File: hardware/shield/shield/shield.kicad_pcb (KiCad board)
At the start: 2 copper layers, 66 x 53.3 mm, 4 parts, among them J1 Power, J2 Digital/PWM, J3 Analog, J4 Digital/PWM

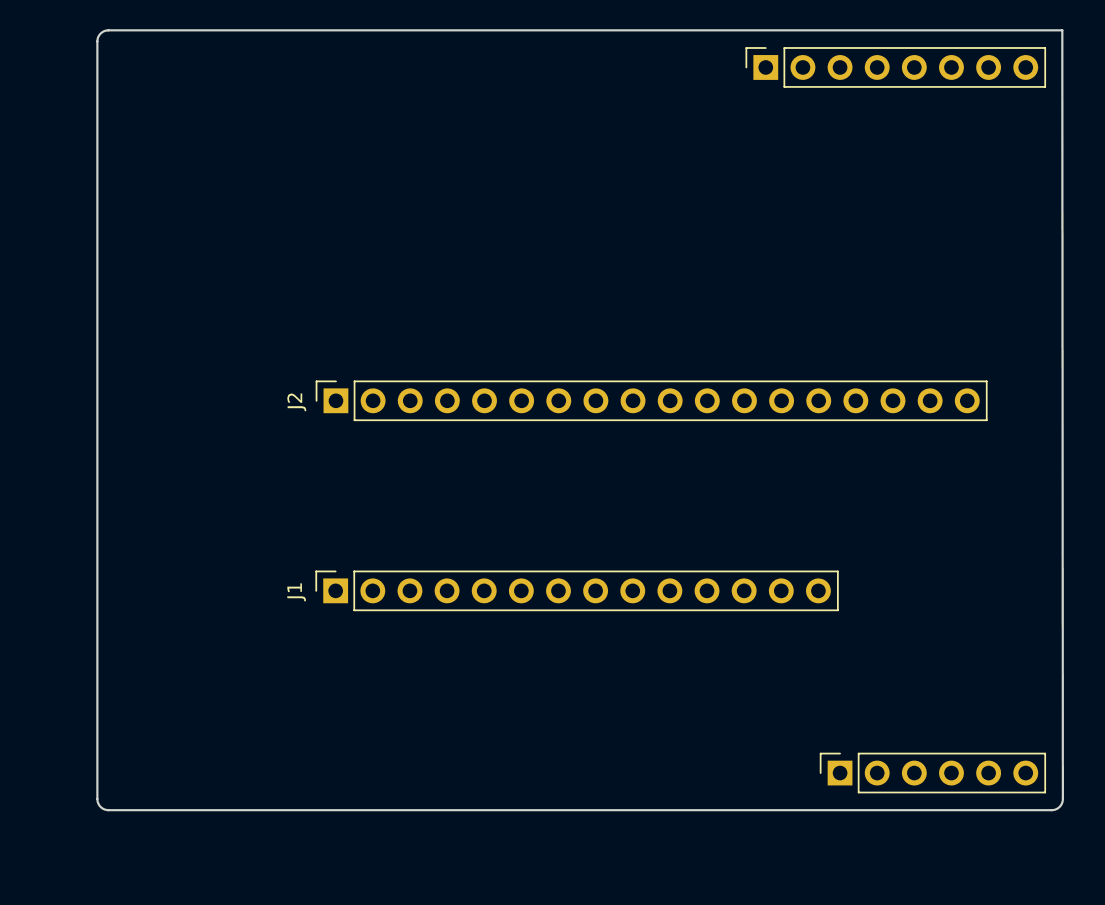
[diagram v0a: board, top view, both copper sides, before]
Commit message: add pins for in/out
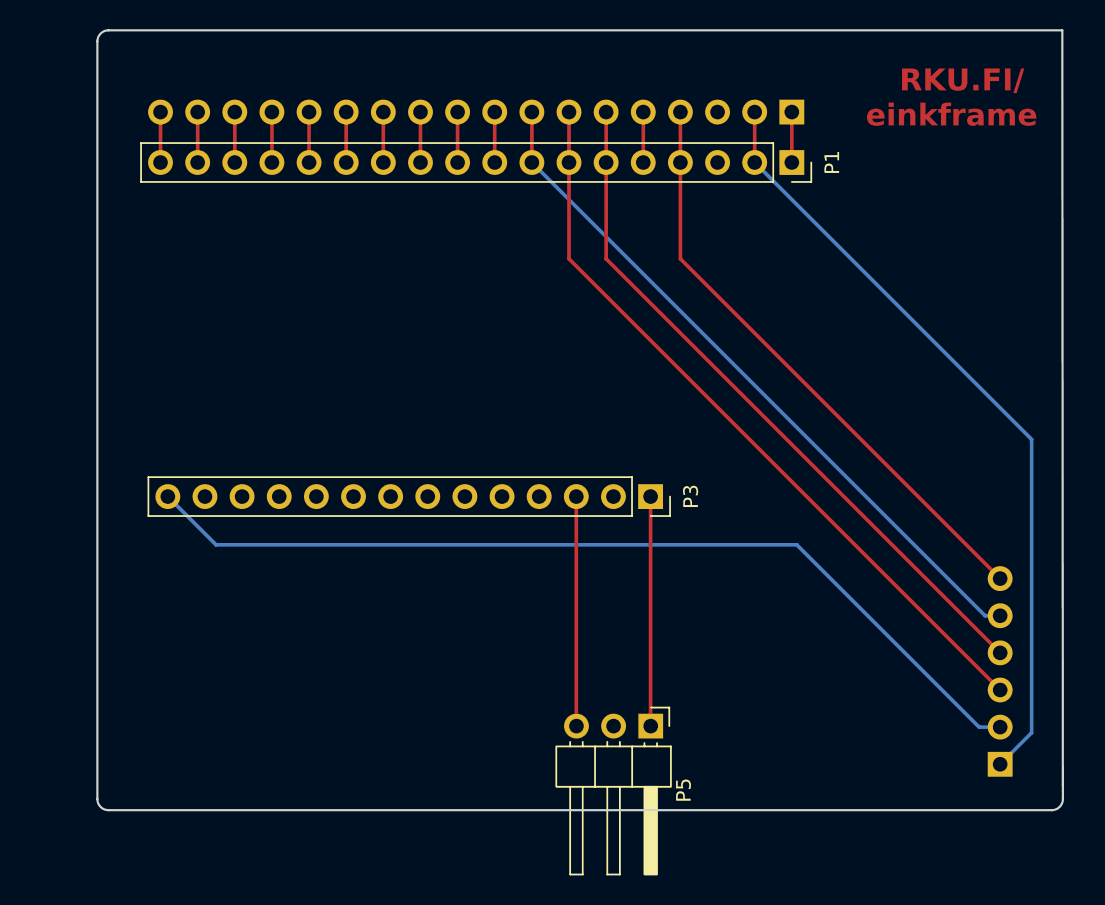
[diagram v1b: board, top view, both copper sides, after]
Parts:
- removed J3: Analog, Connector_PinSocket_2.54mm:PinSocket_1x06_P2.54mm_Vertical
- removed J4: Digital/PWM, Connector_PinSocket_2.54mm:PinSocket_1x08_P2.54mm_Vertical
- added J1: Conn_01x06, Connector_PinHeader_2.54mm:PinHeader_1x06_P2.54mm_Horizontal, B.Cu at (161.8, 96.9)
- added P4: Digital/PWM, Connector_PinHeader_2.54mm:PinHeader_1x18_P2.54mm_Horizontal, B.Cu at (147.5, 52.2)
- added P5: ~, Connector_PinHeader_2.54mm:PinHeader_1x03_P2.54mm_Horizontal, F.Cu at (137.8, 94.2)
- P3: renamed from J1; value Power -> ~
- moved P1 35.2 mm to (147.5, 55.7), turned to -90 degrees
- moved P3 22.5 mm to (137.8, 78.5), turned to -90 degrees
- renumbered J2 to P1
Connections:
- net +5V renamed /IO34/A2
- net /~{RESET} renamed /IO15/A4
- P1 pad 1: unconnected-(J2-Pin_1-Pad1) -> /RST
- P1 pad 10: /12 -> /IO21/SDA
- P1 pad 11: /*11 -> /IO2/D9
- P1 pad 12: /*10 -> /IO13/D7
- P1 pad 13: GND -> /IO14/D6
- P1 pad 14: GND -> /IO0/D5
- P1 pad 15: unconnected-(J2-Pin_15-Pad15) -> /IO26/D3
- P1 pad 16: unconnected-(J2-Pin_16-Pad16) -> /IO25/D2
- P1 pad 17: unconnected-(J2-Pin_17-Pad17) -> /D1(Tx)
- P1 pad 18: unconnected-(J2-Pin_18-Pad18) -> /D0(Rx)
- P1 pad 2: unconnected-(J2-Pin_2-Pad2) -> +3V3
- P1 pad 4: unconnected-(J2-Pin_4-Pad4) -> GND
- P1 pad 5: /SCL/A5 -> /EN
- P1 pad 6: /SDA/A4 -> /IO18/SCK
- P1 pad 7: /AREF -> /IO23/MOSI
- P1 pad 8: GND -> /IO19/MISO
- P1 pad 9: /13 -> /IO22/SCL
- P3 pad 1: unconnected-(J1-Pin_1-Pad1) -> VCC
- P3 pad 10: GND -> /IO36/A0
- P3 pad 11: VCC -> /IO12/D13
- P3 pad 12: unconnected-(J1-Pin_12-Pad12) -> /IO4/D12
- P3 pad 14: unconnected-(J1-Pin_14-Pad14) -> /IO17/D10
- P3 pad 2: unconnected-(J1-Pin_2-Pad2) -> +3V3
- P3 pad 3: unconnected-(J1-Pin_3-Pad3) -> GND
- P3 pad 4: unconnected-(J1-Pin_4-Pad4) -> /IO22/SCL
- P3 pad 5: /IOREF -> /IO21/SDA
- P3 pad 7: +3V3 -> /IO35/A3
- P3 pad 9: GND -> /IO39/A1
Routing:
- net /IO17/D10: track 0.00 -> 63.5 mm
- net GND: track 0.00 -> 56.7 mm
- net +3V3: track 0.00 -> 53.3 mm
- net /IO23/MOSI: track 0.00 -> 51.7 mm
- net /IO19/MISO: track 0.00 -> 48.3 mm
- net /IO18/SCK: track 0.00 -> 48.2 mm
- net VCC: track 0.00 -> 15.7 mm
- net /RST: track 0.00 -> 3.45 mm
- net /IO2/D9: track 0.00 -> 3.45 mm
- net /IO26/D3: track 0.00 -> 3.45 mm
- net /IO25/D2: track 0.00 -> 3.45 mm
- net /IO22/SCL: track 0.00 -> 3.45 mm
- net /IO21/SDA: track 0.00 -> 3.45 mm
- net /IO14/D6: track 0.00 -> 3.45 mm
- net /IO13/D7: track 0.00 -> 3.45 mm
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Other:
- board text added: "RKU.FI/"
- board text added: "einkframe"

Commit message: add shield 0.3.1 version
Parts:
- added P6: ~, Connector_PinHeader_2.54mm:PinHeader_1x03_P2.54mm_Horizontal, F.Cu at (105.5, 89.0)
- added P7: ~, Connector_PinHeader_2.54mm:PinHeader_1x05_P2.54mm_Horizontal, F.Cu at (120.0, 94.2)
- added U1: LF33_TO252, Package_TO_SOT_SMD:TO-252-2, F.Cu at (146.7, 86.8)
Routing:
- net GND: track 56.7 -> 139.7 mm
- net +3.3V: track 0.00 -> 36.1 mm
- net /IO4/D12: track 0.00 -> 15.6 mm
- net /IO36/A0: track 0.00 -> 15.6 mm
- net /IO39/A1: track 0.00 -> 15.6 mm
- net /IO12/D13: track 0.00 -> 15.6 mm
- net VCC: track 15.7 -> 23.3 mm
- net /IO17/D10: track 63.5 -> 65.7 mm
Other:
- board text added: "0.3.1"
